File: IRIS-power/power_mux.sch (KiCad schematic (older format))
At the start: 11 parts

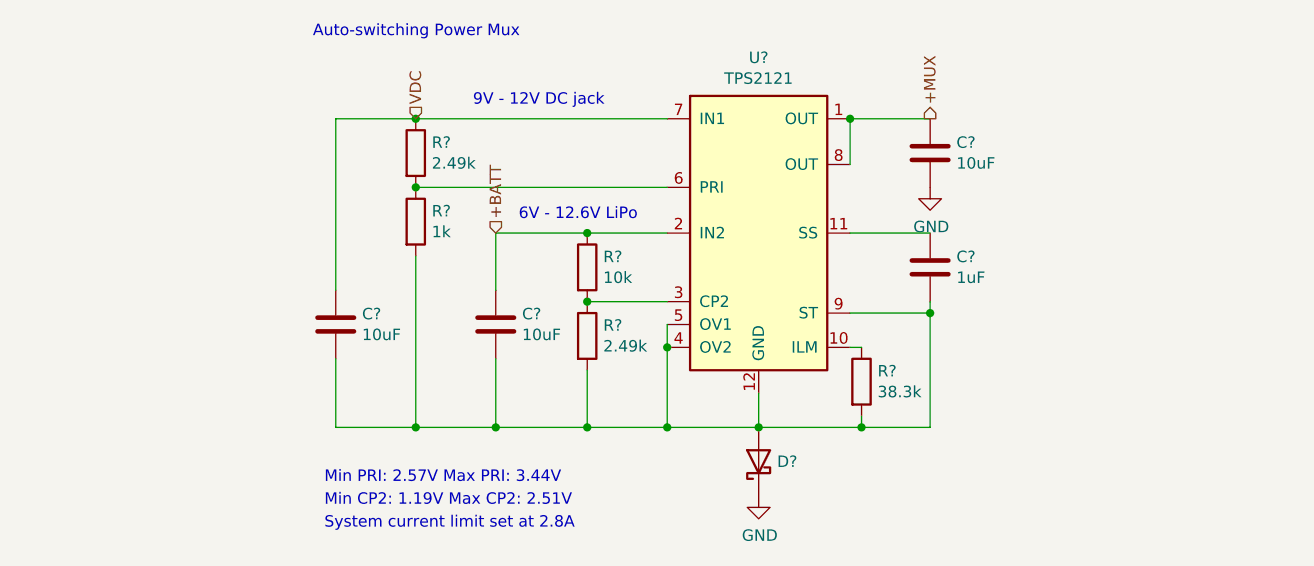
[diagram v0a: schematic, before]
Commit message: Finalized power board V2 schematic, preparing to layout
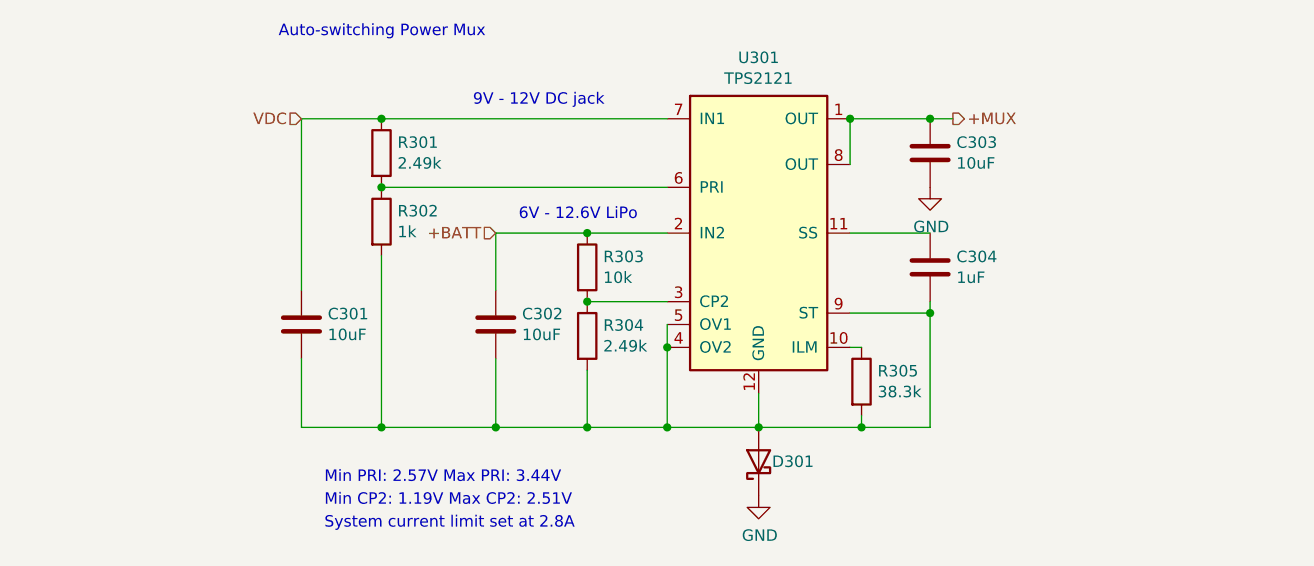
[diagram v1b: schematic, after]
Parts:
- C301, C302, C303: renamed from C?; footprint Capacitor_SMD:C_1206_3216Metric -> Capacitor_SMD:C_0603_1608Metric
- C304: renamed from C?; footprint (none) -> Capacitor_SMD:C_0603_1608Metric
- R301, R302, R305: renamed from R?; footprint (none) -> Resistor_SMD:R_0603_1608Metric
- U301: renamed from U?; footprint (none) -> star-common-lib:TPS2121
- gave numbers to parts that had none: 3
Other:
- moved on the sheet: C301, R301, R302
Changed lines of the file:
@@
 $Descr A4 11693 8268
 encoding utf-8
-Sheet 6 9
+Sheet 3 8
 Title ""
 Date ""
@@
 P 5650 3950
 AR Path="/5F41413C" Ref="R?"  Part="1"
-AR Path="/5F3CE42C/5F41413C" Ref="R?"  Part="1"
-F 0 "R?" H 5720 3996 50  0000 L CNN
+AR Path="/5F3CE42C/5F41413C" Ref="R303"  Part="1"
+F 0 "R303" H 5720 3996 50  0000 L CNN
 F 1 "10k" H 5720 3905 50  0000 L CNN
 F 2 "Resistor_SMD:R_0603_1608Metric" V 5580 3950 50  0001 C CNN
@@
 P 5650 4250
 AR Path="/5F414142" Ref="R?"  Part="1"
-AR Path="/5F3CE42C/5F414142" Ref="R?"  Part="1"
-F 0 "R?" H 5720 4296 50  0000 L CNN
+AR Path="/5F3CE42C/5F414142" Ref="R304"  Part="1"
+F 0 "R304" H 5720 4296 50  0000 L CNN
 F 1 "2.49k" H 5720 4205 50  0000 L CNN
 F 2 "Resistor_SMD:R_0603_1608Metric" V 5580 4250 50  0001 C CNN
@@
 Connection ~ 6000 4650
 Wire Wire Line
-	4900 3900 4900 4650
-Connection ~ 4900 3300
+	4750 3900 4750 4650
+Connection ~ 4750 3300
 Wire Wire Line
 	6800 3500 6800 3300
@@
 L Device:C C?
 U 1 1 5F414151
-P 4550 4200
+P 4400 4200
 AR Path="/5F414151" Ref="C?"  Part="1"
-AR Path="/5F3CE42C/5F414151" Ref="C?"  Part="1"
-F 0 "C?" H 4665 4246 50  0000 L CNN
-F 1 "10uF" H 4665 4155 50  0000 L CNN
-F 2 "Capacitor_SMD:C_1206_3216Metric" H 4588 4050 50  0001 C CNN
-F 3 "~" H 4550 4200 50  0001 C CNN
-	1    4550 4200
+AR Path="/5F3CE42C/5F414151" Ref="C301"  Part="1"
+F 0 "C301" H 4515 4246 50  0000 L CNN
+F 1 "10uF" H 4515 4155 50  0000 L CNN
+F 2 "Capacitor_SMD:C_0603_1608Metric" H 4438 4050 50  0001 C CNN
+F 3 "~" H 4400 4200 50  0001 C CNN
+	1    4400 4200
 	1    0    0    -1
 $EndComp
@@
 P 5250 4200
 AR Path="/5F414157" Ref="C?"  Part="1"
-AR Path="/5F3CE42C/5F414157" Ref="C?"  Part="1"
-F 0 "C?" H 5365 4246 50  0000 L CNN
+AR Path="/5F3CE42C/5F414157" Ref="C302"  Part="1"
+F 0 "C302" H 5365 4246 50  0000 L CNN
 F 1 "10uF" H 5365 4155 50  0000 L CNN
-F 2 "Capacitor_SMD:C_1206_3216Metric" H 5288 4050 50  0001 C CNN
+F 2 "Capacitor_SMD:C_0603_1608Metric" H 5288 4050 50  0001 C CNN
 F 3 "~" H 5250 4200 50  0001 C CNN
 	1    5250 4200
@@
 	5250 4350 5250 4650
 Wire Wire Line
-	4550 4050 4550 3300
-Wire Wire Line
-	4550 3300 4900 3300
-Wire Wire Line
-	4550 4350 4550 4650
-Wire Wire Line
-	4550 4650 4900 4650
-Connection ~ 4900 4650
+	4400 4050 4400 3300
+Wire Wire Line
+	4400 3300 4750 3300
+Wire Wire Line
+	4400 4350 4400 4650
+Wire Wire Line
+	4400 4650 4750 4650
+Connection ~ 4750 4650
 $Comp
 L Device:C C?
@@
 P 7150 3450
 AR Path="/5F414163" Ref="C?"  Part="1"
-AR Path="/5F3CE42C/5F414163" Ref="C?"  Part="1"
-F 0 "C?" H 7265 3496 50  0000 L CNN
+AR Path="/5F3CE42C/5F414163" Ref="C303"  Part="1"
+F 0 "C303" H 7265 3496 50  0000 L CNN
 F 1 "10uF" H 7265 3405 50  0000 L CNN
-F 2 "Capacitor_SMD:C_1206_3216Metric" H 7188 3300 50  0001 C CNN
+F 2 "Capacitor_SMD:C_0603_1608Metric" H 7188 3300 50  0001 C CNN
 F 3 "~" H 7150 3450 50  0001 C CNN
 	1    7150 3450
@@
 P 6400 3850
 AR Path="/5F41416A" Ref="U?"  Part="1"
-AR Path="/5F3CE42C/5F41416A" Ref="U?"  Part="1"
-F 0 "U?" H 6400 4667 50  0000 C CNN
+AR Path="/5F3CE42C/5F41416A" Ref="U301"  Part="1"
+F 0 "U301" H 6400 4667 50  0000 C CNN
 F 1 "TPS2121" H 6400 4576 50  0000 C CNN
-F 2 "" H 6400 3950 50  0001 C CNN
+F 2 "star-common-lib:TPS2121" H 6400 3950 50  0001 C CNN
 F 3 "" H 6400 3950 50  0001 C CNN
 	1    6400 3850
@@
 P 7150 3950
 AR Path="/5F414179" Ref="C?"  Part="1"
-AR Path="/5F3CE42C/5F414179" Ref="C?"  Part="1"
-F 0 "C?" H 7265 3996 50  0000 L CNN
+AR Path="/5F3CE42C/5F414179" Ref="C304"  Part="1"
+F 0 "C304" H 7265 3996 50  0000 L CNN
 F 1 "1uF" H 7265 3905 50  0000 L CNN
-F 2 "" H 7188 3800 50  0001 C CNN
+F 2 "Capacitor_SMD:C_0603_1608Metric" H 7188 3800 50  0001 C CNN
 F 3 "~" H 7150 3950 50  0001 C CNN
 	1    7150 3950
@@
 P 6850 4450
 AR Path="/5F41417F" Ref="R?"  Part="1"
-AR Path="/5F3CE42C/5F41417F" Ref="R?"  Part="1"
-F 0 "R?" H 6920 4496 50  0000 L CNN
+AR Path="/5F3CE42C/5F41417F" Ref="R305"  Part="1"
+F 0 "R305" H 6920 4496 50  0000 L CNN
 F 1 "38.3k" H 6920 4405 50  0000 L CNN
-F 2 "" V 6780 4450 50  0001 C CNN
+F 2 "Resistor_SMD:R_0603_1608Metric" V 6780 4450 50  0001 C CNN
 F 3 "~" H 6850 4450 50  0001 C CNN
 	1    6850 4450
 	1    0    0    -1
 $EndComp
-Connection ~ 5250 4650
-Wire Wire Line
-	4900 4650 5250 4650
 Wire Wire Line
 	5250 4050 5250 3800
@@
 	5250 3800 5650 3800
 Connection ~ 5650 3800
-Wire Wire Line
-	4900 3600 6000 3600
-Wire Wire Line
-	4900 3300 6000 3300
 Text Notes 5150 3250 0    50   ~ 0
 9V - 12V DC jack
@@
 L Device:R R?
 U 1 1 5F41419A
-P 4900 3450
+P 4750 3450
 AR Path="/5F41419A" Ref="R?"  Part="1"
-AR Path="/5F3CE42C/5F41419A" Ref="R?"  Part="1"
-F 0 "R?" H 4970 3496 50  0000 L CNN
-F 1 "2.49k" H 4970 3405 50  0000 L CNN
-F 2 "" V 4830 3450 50  0001 C CNN
-F 3 "~" H 4900 3450 50  0001 C CNN
-	1    4900 3450
+AR Path="/5F3CE42C/5F41419A" Ref="R301"  Part="1"
+F 0 "R301" H 4820 3496 50  0000 L CNN
+F 1 "2.49k" H 4820 3405 50  0000 L CNN
+F 2 "Resistor_SMD:R_0603_1608Metric" V 4680 3450 50  0001 C CNN
+F 3 "~" H 4750 3450 50  0001 C CNN
+	1    4750 3450
 	1    0    0    -1
 $EndComp
@@
 L Device:R R?
 U 1 1 5F4141A0
-P 4900 3750
+P 4750 3750
 AR Path="/5F4141A0" Ref="R?"  Part="1"
-AR Path="/5F3CE42C/5F4141A0" Ref="R?"  Part="1"
-F 0 "R?" H 4970 3796 50  0000 L CNN
-F 1 "1k" H 4970 3705 50  0000 L CNN
-F 2 "" V 4830 3750 50  0001 C CNN
-F 3 "~" H 4900 3750 50  0001 C CNN
-	1    4900 3750
-	1    0    0    -1
-$EndComp
-Connection ~ 4900 3600
-Text Notes 4450 2950 0    50   ~ 0
+AR Path="/5F3CE42C/5F4141A0" Ref="R302"  Part="1"
+F 0 "R302" H 4820 3796 50  0000 L CNN
+F 1 "1k" H 4820 3705 50  0000 L CNN
+F 2 "Resistor_SMD:R_0603_1608Metric" V 4680 3750 50  0001 C CNN
+F 3 "~" H 4750 3750 50  0001 C CNN
+	1    4750 3750
+	1    0    0    -1
+$EndComp
+Connection ~ 4750 3600
+Text Notes 4300 2950 0    50   ~ 0
 Auto-switching Power Mux
 $Comp
@@
 P 7150 3600
 AR Path="/5F4141A9" Ref="#PWR?"  Part="1"
-AR Path="/5F3CE42C/5F4141A9" Ref="#PWR?"  Part="1"
-F 0 "#PWR?" H 7150 3350 50  0001 C CNN
+AR Path="/5F3CE42C/5F4141A9" Ref="#PWR0302"  Part="1"
+F 0 "#PWR0302" H 7150 3350 50  0001 C CNN
 F 1 "GND" H 7155 3427 50  0000 C CNN
 F 2 "" H 7150 3600 50  0001 C CNN
@@
 P 6400 4950
 AR Path="/5F4141B6" Ref="#PWR?"  Part="1"
-AR Path="/5F3CE42C/5F4141B6" Ref="#PWR?"  Part="1"
-F 0 "#PWR?" H 6400 4700 50  0001 C CNN
+AR Path="/5F3CE42C/5F4141B6" Ref="#PWR0301"  Part="1"
+F 0 "#PWR0301" H 6400 4700 50  0001 C CNN
 F 1 "GND" H 6405 4777 50  0000 C CNN
 F 2 "" H 6400 4950 50  0001 C CNN
@@
 P 6400 4800
 AR Path="/5F4141C2" Ref="D?"  Part="1"
-AR Path="/5F3CE42C/5F4141C2" Ref="D?"  Part="1"
-F 0 "D?" V 6400 4675 50  0000 C CNN
+AR Path="/5F3CE42C/5F4141C2" Ref="D301"  Part="1"
+F 0 "D301" V 6400 4650 50  0000 C CNN
 F 1 "D_Schottky" H 6400 4674 50  0001 C CNN
 F 2 "Diode_SMD:D_SMA_Handsoldering" H 6400 4800 50  0001 C CNN
@@
 	0    -1   -1   0
 $EndComp
-Text HLabel 4900 3300 1    50   Input ~ 0
+Text HLabel 4400 3300 0    50   Input ~ 0
 VDC
-Text HLabel 7150 3300 1    50   Output ~ 0
+Text HLabel 7250 3300 2    50   Output ~ 0
 +MUX
-Text HLabel 5250 3800 1    50   Input ~ 0
+Text HLabel 5250 3800 0    50   Input ~ 0
 +BATT
+Wire Wire Line
+	4750 3300 6000 3300
+Wire Wire Line
+	4750 3600 6000 3600
+Wire Wire Line
+	4750 4650 5250 4650
+Connection ~ 5250 4650
+Wire Wire Line
+	7250 3300 7150 3300
+Connection ~ 7150 3300
 $EndSCHEMATC

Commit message: Updated layout
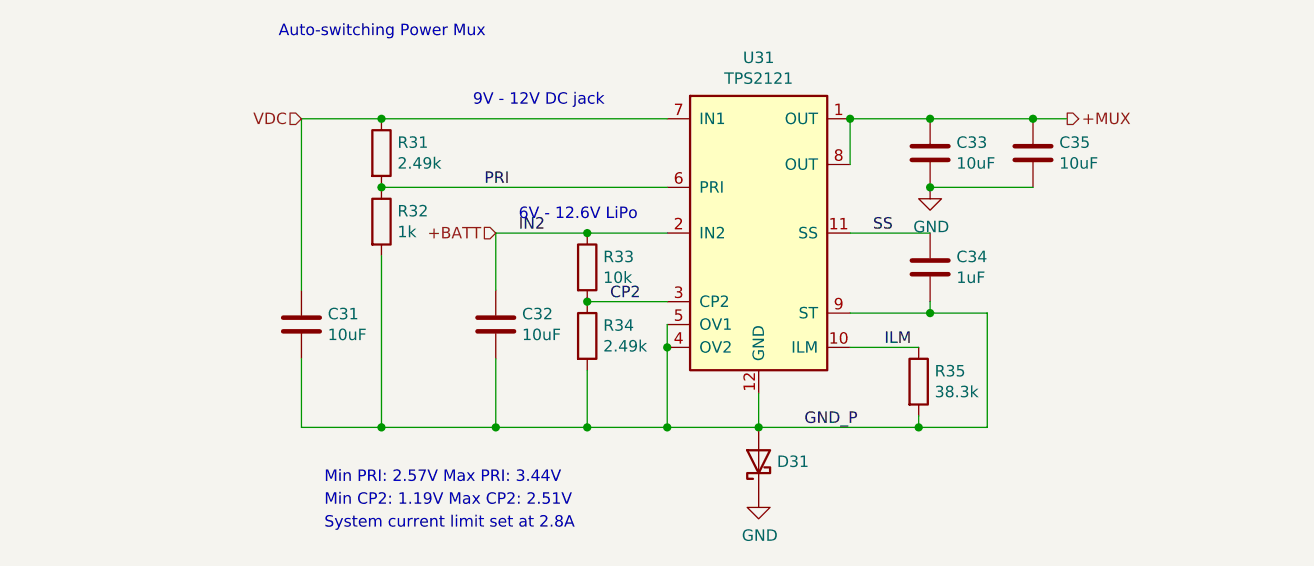
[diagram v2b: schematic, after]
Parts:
- added C35: 10uF, Capacitor_SMD:C_0603_1608Metric, symbol Device:C
- renumbered C301 to C31, C302 to C32, C303 to C33, C304 to C34, D301 to D31, R301 to R31, R302 to R32, R303 to R33, R304 to R34, R305 to R35, U301 to U31
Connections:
- net +MUX: now also C35.1
- net GND: now also C35.2
- net CP2: now reaches R33.2, R34.1, U31.3 (CP2)
- net GND_P: now reaches C31.2, C32.2, C34.2, D31.2 (A), R32.2, R34.2, R35.2, U31.12 (GND), U31.4 (OV2), U31.5 (OV1), U31.9 (ST)
- net ILM: now reaches R35.1, U31.10 (ILM)
- net SS: now reaches C34.1, U31.11 (SS)
- net PRI: now reaches R31.2, R32.1, U31.6 (PRI)
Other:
- moved on the sheet: R35
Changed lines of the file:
@@
 $EndDescr
-Wire Wire Line
-	6850 4300 6800 4300
 Wire Wire Line
 	6000 4650 6400 4650
@@
 P 5650 3950
 AR Path="/5F41413C" Ref="R?"  Part="1"
-AR Path="/5F3CE42C/5F41413C" Ref="R303"  Part="1"
-F 0 "R303" H 5720 3996 50  0000 L CNN
+AR Path="/5F3CE42C/5F41413C" Ref="R33"  Part="1"
+F 0 "R33" H 5720 3996 50  0000 L CNN
 F 1 "10k" H 5720 3905 50  0000 L CNN
 F 2 "Resistor_SMD:R_0603_1608Metric" V 5580 3950 50  0001 C CNN
@@
 P 5650 4250
 AR Path="/5F414142" Ref="R?"  Part="1"
-AR Path="/5F3CE42C/5F414142" Ref="R304"  Part="1"
-F 0 "R304" H 5720 4296 50  0000 L CNN
+AR Path="/5F3CE42C/5F414142" Ref="R34"  Part="1"
+F 0 "R34" H 5720 4296 50  0000 L CNN
 F 1 "2.49k" H 5720 4205 50  0000 L CNN
 F 2 "Resistor_SMD:R_0603_1608Metric" V 5580 4250 50  0001 C CNN
@@
 P 4400 4200
 AR Path="/5F414151" Ref="C?"  Part="1"
-AR Path="/5F3CE42C/5F414151" Ref="C301"  Part="1"
-F 0 "C301" H 4515 4246 50  0000 L CNN
+AR Path="/5F3CE42C/5F414151" Ref="C31"  Part="1"
+F 0 "C31" H 4515 4246 50  0000 L CNN
 F 1 "10uF" H 4515 4155 50  0000 L CNN
 F 2 "Capacitor_SMD:C_0603_1608Metric" H 4438 4050 50  0001 C CNN
@@
 P 5250 4200
 AR Path="/5F414157" Ref="C?"  Part="1"
-AR Path="/5F3CE42C/5F414157" Ref="C302"  Part="1"
-F 0 "C302" H 5365 4246 50  0000 L CNN
+AR Path="/5F3CE42C/5F414157" Ref="C32"  Part="1"
+F 0 "C32" H 5365 4246 50  0000 L CNN
 F 1 "10uF" H 5365 4155 50  0000 L CNN
 F 2 "Capacitor_SMD:C_0603_1608Metric" H 5288 4050 50  0001 C CNN
@@
 P 7150 3450
 AR Path="/5F414163" Ref="C?"  Part="1"
-AR Path="/5F3CE42C/5F414163" Ref="C303"  Part="1"
-F 0 "C303" H 7265 3496 50  0000 L CNN
+AR Path="/5F3CE42C/5F414163" Ref="C33"  Part="1"
+F 0 "C33" H 7265 3496 50  0000 L CNN
 F 1 "10uF" H 7265 3405 50  0000 L CNN
 F 2 "Capacitor_SMD:C_0603_1608Metric" H 7188 3300 50  0001 C CNN
@@
 P 6400 3850
 AR Path="/5F41416A" Ref="U?"  Part="1"
-AR Path="/5F3CE42C/5F41416A" Ref="U301"  Part="1"
-F 0 "U301" H 6400 4667 50  0000 C CNN
+AR Path="/5F3CE42C/5F41416A" Ref="U31"  Part="1"
+F 0 "U31" H 6400 4667 50  0000 C CNN
 F 1 "TPS2121" H 6400 4576 50  0000 C CNN
 F 2 "star-common-lib:TPS2121" H 6400 3950 50  0001 C CNN
@@
 P 7150 3950
 AR Path="/5F414179" Ref="C?"  Part="1"
-AR Path="/5F3CE42C/5F414179" Ref="C304"  Part="1"
-F 0 "C304" H 7265 3996 50  0000 L CNN
+AR Path="/5F3CE42C/5F414179" Ref="C34"  Part="1"
+F 0 "C34" H 7265 3996 50  0000 L CNN
 F 1 "1uF" H 7265 3905 50  0000 L CNN
 F 2 "Capacitor_SMD:C_0603_1608Metric" H 7188 3800 50  0001 C CNN
@@
 L Device:R R?
 U 1 1 5F41417F
-P 6850 4450
+P 7100 4450
 AR Path="/5F41417F" Ref="R?"  Part="1"
-AR Path="/5F3CE42C/5F41417F" Ref="R305"  Part="1"
-F 0 "R305" H 6920 4496 50  0000 L CNN
-F 1 "38.3k" H 6920 4405 50  0000 L CNN
-F 2 "Resistor_SMD:R_0603_1608Metric" V 6780 4450 50  0001 C CNN
-F 3 "~" H 6850 4450 50  0001 C CNN
-	1    6850 4450
+AR Path="/5F3CE42C/5F41417F" Ref="R35"  Part="1"
+F 0 "R35" H 7170 4496 50  0000 L CNN
+F 1 "38.3k" H 7170 4405 50  0000 L CNN
+F 2 "Resistor_SMD:R_0603_1608Metric" V 7030 4450 50  0001 C CNN
+F 3 "~" H 7100 4450 50  0001 C CNN
+	1    7100 4450
 	1    0    0    -1
 $EndComp
@@
 6V - 12.6V LiPo
 Wire Wire Line
-	6400 4650 6850 4650
-Wire Wire Line
-	6850 4600 6850 4650
-Connection ~ 6850 4650
+	7100 4600 7100 4650
+Connection ~ 7100 4650
 $Comp
 L Device:R R?
@@
 P 4750 3450
 AR Path="/5F41419A" Ref="R?"  Part="1"
-AR Path="/5F3CE42C/5F41419A" Ref="R301"  Part="1"
-F 0 "R301" H 4820 3496 50  0000 L CNN
+AR Path="/5F3CE42C/5F41419A" Ref="R31"  Part="1"
+F 0 "R31" H 4820 3496 50  0000 L CNN
 F 1 "2.49k" H 4820 3405 50  0000 L CNN
 F 2 "Resistor_SMD:R_0603_1608Metric" V 4680 3450 50  0001 C CNN
@@
 P 4750 3750
 AR Path="/5F4141A0" Ref="R?"  Part="1"
-AR Path="/5F3CE42C/5F4141A0" Ref="R302"  Part="1"
-F 0 "R302" H 4820 3796 50  0000 L CNN
+AR Path="/5F3CE42C/5F4141A0" Ref="R32"  Part="1"
+F 0 "R32" H 4820 3796 50  0000 L CNN
 F 1 "1k" H 4820 3705 50  0000 L CNN
 F 2 "Resistor_SMD:R_0603_1608Metric" V 4680 3750 50  0001 C CNN
@@
 P 7150 3600
 AR Path="/5F4141A9" Ref="#PWR?"  Part="1"
-AR Path="/5F3CE42C/5F4141A9" Ref="#PWR0302"  Part="1"
-F 0 "#PWR0302" H 7150 3350 50  0001 C CNN
+AR Path="/5F3CE42C/5F4141A9" Ref="#PWR032"  Part="1"
+F 0 "#PWR032" H 7150 3350 50  0001 C CNN
 F 1 "GND" H 7155 3427 50  0000 C CNN
 F 2 "" H 7150 3600 50  0001 C CNN
@@
 $EndComp
 Wire Wire Line
-	6850 4650 7150 4650
+	7100 4650 7400 4650
 Wire Wire Line
 	7150 3800 6800 3800
@@
 	6800 4150 7150 4150
 Wire Wire Line
-	7150 4150 7150 4650
+	7400 4150 7400 4650
 Wire Wire Line
 	7150 4150 7150 4100
-Connection ~ 7150 4150
 $Comp
 L power:GND #PWR?
@@
 P 6400 4950
 AR Path="/5F4141B6" Ref="#PWR?"  Part="1"
-AR Path="/5F3CE42C/5F4141B6" Ref="#PWR0301"  Part="1"
-F 0 "#PWR0301" H 6400 4700 50  0001 C CNN
+AR Path="/5F3CE42C/5F4141B6" Ref="#PWR031"  Part="1"
+F 0 "#PWR031" H 6400 4700 50  0001 C CNN
 F 1 "GND" H 6405 4777 50  0000 C CNN
 F 2 "" H 6400 4950 50  0001 C CNN
@@
 P 6400 4800
 AR Path="/5F4141C2" Ref="D?"  Part="1"
-AR Path="/5F3CE42C/5F4141C2" Ref="D301"  Part="1"
-F 0 "D301" V 6400 4650 50  0000 C CNN
+AR Path="/5F3CE42C/5F4141C2" Ref="D31"  Part="1"
+F 0 "D31" V 6400 4650 50  0000 C CNN
 F 1 "D_Schottky" H 6400 4674 50  0001 C CNN
 F 2 "Diode_SMD:D_SMA_Handsoldering" H 6400 4800 50  0001 C CNN
@@
 Text HLabel 4400 3300 0    50   Input ~ 0
 VDC
-Text HLabel 7250 3300 2    50   Output ~ 0
+Text HLabel 7750 3300 2    50   Output ~ 0
 +MUX
 Text HLabel 5250 3800 0    50   Input ~ 0
@@
 	4750 4650 5250 4650
 Connection ~ 5250 4650
-Wire Wire Line
-	7250 3300 7150 3300
 Connection ~ 7150 3300
+Text Label 5200 3600 0    50   ~ 0
+PRI
+Text Label 5350 3800 0    50   ~ 0
+IN2
+Text Label 5750 4100 0    50   ~ 0
+CP2
+Text Label 6900 3800 0    50   ~ 0
+SS
+Wire Wire Line
+	6800 4300 7100 4300
+Wire Wire Line
+	6400 4650 7100 4650
+Wire Wire Line
+	7150 4150 7400 4150
+Connection ~ 7150 4150
+Text Label 6950 4300 0    50   ~ 0
+ILM
+Text Label 6600 4650 0    50   ~ 0
+GND_P
+Wire Wire Line
+	7150 3300 7600 3300
+$Comp
+L Device:C C?
+U 1 1 5F3831BE
+P 7600 3450
+AR Path="/5F3831BE" Ref="C?"  Part="1"
+AR Path="/5F3CE42C/5F3831BE" Ref="C35"  Part="1"
+F 0 "C35" H 7715 3496 50  0000 L CNN
+F 1 "10uF" H 7715 3405 50  0000 L CNN
+F 2 "Capacitor_SMD:C_0603_1608Metric" H 7638 3300 50  0001 C CNN
+F 3 "~" H 7600 3450 50  0001 C CNN
+	1    7600 3450
+	1    0    0    -1
+$EndComp
+Connection ~ 7600 3300
+Wire Wire Line
+	7600 3300 7750 3300
+Wire Wire Line
+	7600 3600 7150 3600
+Connection ~ 7150 3600
 $EndSCHEMATC

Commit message: Improved fuel gauge layout
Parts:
- C31, C32, C33, C35: Digikey PN (none) -> 1276-1192-1-ND
- C34: Digikey PN (none) -> 1276-1102-1-ND
- R32: Digikey PN (none) -> RMCF0603FT1K00CT-ND
- R33: Digikey PN (none) -> RNCP0603FTD10K0CT-ND
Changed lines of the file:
@@
 F 2 "Resistor_SMD:R_0603_1608Metric" V 5580 3950 50  0001 C CNN
 F 3 "~" H 5650 3950 50  0001 C CNN
+F 4 "RNCP0603FTD10K0CT-ND" H 5650 3950 50  0001 C CNN "Digikey PN"
 	1    5650 3950
 	1    0    0    -1
@@
 F 2 "Capacitor_SMD:C_0603_1608Metric" H 4438 4050 50  0001 C CNN
 F 3 "~" H 4400 4200 50  0001 C CNN
+F 4 "1276-1192-1-ND" H 4400 4200 50  0001 C CNN "Digikey PN"
 	1    4400 4200
 	1    0    0    -1
@@
 F 2 "Capacitor_SMD:C_0603_1608Metric" H 5288 4050 50  0001 C CNN
 F 3 "~" H 5250 4200 50  0001 C CNN
+F 4 "1276-1192-1-ND" H 5250 4200 50  0001 C CNN "Digikey PN"
 	1    5250 4200
 	1    0    0    -1
@@
 F 2 "Capacitor_SMD:C_0603_1608Metric" H 7188 3300 50  0001 C CNN
 F 3 "~" H 7150 3450 50  0001 C CNN
+F 4 "1276-1192-1-ND" H 7150 3450 50  0001 C CNN "Digikey PN"
 	1    7150 3450
 	1    0    0    -1
@@
 F 2 "Capacitor_SMD:C_0603_1608Metric" H 7188 3800 50  0001 C CNN
 F 3 "~" H 7150 3950 50  0001 C CNN
+F 4 "1276-1102-1-ND" H 7150 3950 50  0001 C CNN "Digikey PN"
 	1    7150 3950
 	1    0    0    -1
@@
 F 2 "Resistor_SMD:R_0603_1608Metric" V 4680 3750 50  0001 C CNN
 F 3 "~" H 4750 3750 50  0001 C CNN
+F 4 "RMCF0603FT1K00CT-ND" H 4750 3750 50  0001 C CNN "Digikey PN"
 	1    4750 3750
 	1    0    0    -1
@@
 F 2 "Capacitor_SMD:C_0603_1608Metric" H 7638 3300 50  0001 C CNN
 F 3 "~" H 7600 3450 50  0001 C CNN
+F 4 "1276-1192-1-ND" H 7600 3450 50  0001 C CNN "Digikey PN"
 	1    7600 3450
 	1    0    0    -1
